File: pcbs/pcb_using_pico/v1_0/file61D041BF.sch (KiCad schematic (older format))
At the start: 10 parts, among them J2 Conn_01x03_Female, M1 P-CHANNEL-MOSFET, U4 ESP32-WROOM-32

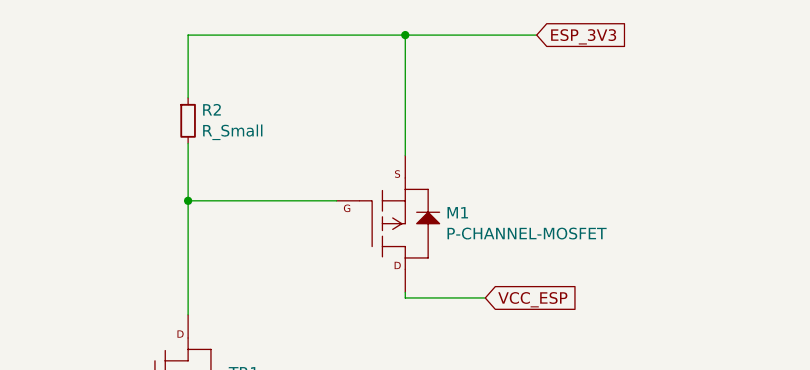
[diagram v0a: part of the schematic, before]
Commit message: V2.0 sent off for fab. New charger IC with more solderable footprint, plus other fixes
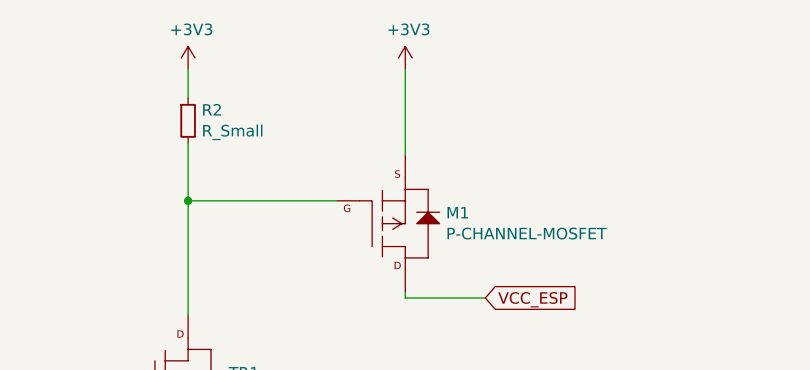
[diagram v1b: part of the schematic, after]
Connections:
- net ESP_3V3 renamed +3V3
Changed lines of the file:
@@
 Wire Wire Line
 	1525 2375 1400 2375
+$Comp
+L power:+3V3 #PWR0120
+U 1 1 61D53982
+P 1950 900
+F 0 "#PWR0120" H 1950 750 50  0001 C CNN
+F 1 "+3V3" H 1965 1073 50  0000 C CNN
+F 2 "" H 1950 900 50  0001 C CNN
+F 3 "" H 1950 900 50  0001 C CNN
+	1    1950 900
+	1    0    0    -1
+$EndComp
+Wire Wire Line
+	1950 900  1950 1025
 Wire Wire Line
 	1950 1225 1950 1475
@@
 Wire Wire Line
 	1950 1475 1950 1975
+$Comp
+L power:+3V3 #PWR0121
+U 1 1 61D55748
+P 2900 900
+F 0 "#PWR0121" H 2900 750 50  0001 C CNN
+F 1 "+3V3" H 2915 1073 50  0000 C CNN
+F 2 "" H 2900 900 50  0001 C CNN
+F 3 "" H 2900 900 50  0001 C CNN
+	1    2900 900
+	1    0    0    -1
+$EndComp
+Wire Wire Line
+	2900 900  2900 1275
 Text GLabel 3250 1900 2    50   Input ~ 0
 VCC_ESP
@@
 	1    0    0    -1
 $EndComp
-Text GLabel 3475 750  2    50   Input ~ 0
-ESP_3V3
-Wire Wire Line
-	3475 750  2900 750
-Wire Wire Line
-	2900 750  2900 1275
-Wire Wire Line
-	2900 750  1950 750
-Wire Wire Line
-	1950 750  1950 1025
-Connection ~ 2900 750
 $EndSCHEMATC
